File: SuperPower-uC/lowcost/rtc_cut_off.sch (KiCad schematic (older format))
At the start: 12 parts, among them Q1 2N7002, U7 PCF8563T, U8 XC6206P332MR, U9 TCA6408A, Y2 32.768KHz

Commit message: changed int io to directely connect to int bus
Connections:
- wire segments 59 -> 56
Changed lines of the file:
@@
 Text GLabel 5950 3550 2    50   Input ~ 0
 exp4
-Text GLabel 4550 3050 0    50   Input ~ 0
+Text GLabel 3750 2900 0    50   Input ~ 0
 INT_IO
 Wire Wire Line
@@
 Wire Wire Line
 	4650 3250 5100 3250
-Wire Wire Line
-	4550 3050 4600 3050
-Wire Wire Line
-	4600 3050 4600 3150
 Text GLabel 4650 3250 0    50   Input ~ 0
 3v3_EN
@@
 	1    0    0    -1
 $EndComp
-Connection ~ 4600 3150
-Wire Wire Line
-	4600 3150 4250 3150
-Wire Wire Line
-	4600 3150 5100 3150
 Wire Wire Line
 	4750 3050 5100 3050
@@
 Text Label 5050 2750 2    50   ~ 0
 V_I2C
+Wire Wire Line
+	4250 3150 5100 3150
 $EndSCHEMATC

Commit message: connected espander address pin to VBAT
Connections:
- wire segments 56 -> 55
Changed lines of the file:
@@
 Wire Wire Line
 	5100 2850 5050 2850
-Wire Wire Line
-	5050 2850 5050 2950
-Wire Wire Line
-	5050 2950 5100 2950
 $Comp
 L power:GND #PWR0109
@@
 	5600 4750 6100 4750
 Connection ~ 6100 4750
-Connection ~ 5050 2850
 Text Label 1750 850  2    50   ~ 0
 SDA
@@
 Wire Wire Line
 	4250 3150 5100 3150
+Text Label 4900 2950 0    50   ~ 0
+VBAT
+Wire Wire Line
+	4900 2950 5100 2950
 $EndSCHEMATC

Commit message: connected vccd of io expander to 3v3 i2c and added bypass cap
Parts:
- added C22: 0.1µF, Capacitor_SMD:C_0603_1608Metric_Pad1.05x0.95mm_HandSolder, symbol Device:C
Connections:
- wire segments 55 -> 58
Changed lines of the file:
@@
 Wire Wire Line
 	5900 3050 6150 3050
-Text Label 6150 2850 2    50   ~ 0
-VBAT
-Wire Wire Line
-	5900 2850 6150 2850
 Text Label 8650 2900 2    50   ~ 0
 SDA
@@
 Wire Wire Line
 	4250 3150 5100 3150
-Text Label 4900 2950 0    50   ~ 0
-VBAT
-Wire Wire Line
-	4900 2950 5100 2950
+Wire Wire Line
+	5100 2950 5050 2950
+Wire Wire Line
+	5050 2950 5050 2850
+Connection ~ 5050 2850
+Text Label 6450 2850 2    50   ~ 0
+V_I2C
+$Comp
+L Device:C C22
+U 1 1 5FC9C8EC
+P 6450 3050
+F 0 "C22" H 6300 2950 50  0000 L CNN
+F 1 "0.1µF" H 6200 3150 50  0000 L CNN
+F 2 "Capacitor_SMD:C_0603_1608Metric_Pad1.05x0.95mm_HandSolder" H 6488 2900 50  0001 C CNN
+F 3 "~" H 6450 3050 50  0001 C CNN
+F 4 "C14858" H 6450 3050 50  0001 C CNN "LCSC"
+	1    6450 3050
+	-1   0    0    1
+$EndComp
+Wire Wire Line
+	5900 2850 6450 2850
+$Comp
+L power:GND #PWR?
+U 1 1 5FCA03ED
+P 6450 3250
+F 0 "#PWR?" H 6450 3000 50  0001 C CNN
+F 1 "GND" H 6455 3077 50  0000 C CNN
+F 2 "" H 6450 3250 50  0001 C CNN
+F 3 "" H 6450 3250 50  0001 C CNN
+	1    6450 3250
+	1    0    0    -1
+$EndComp
+Wire Wire Line
+	6450 3250 6450 3200
+Wire Wire Line
+	6450 2900 6450 2850
 $EndSCHEMATC

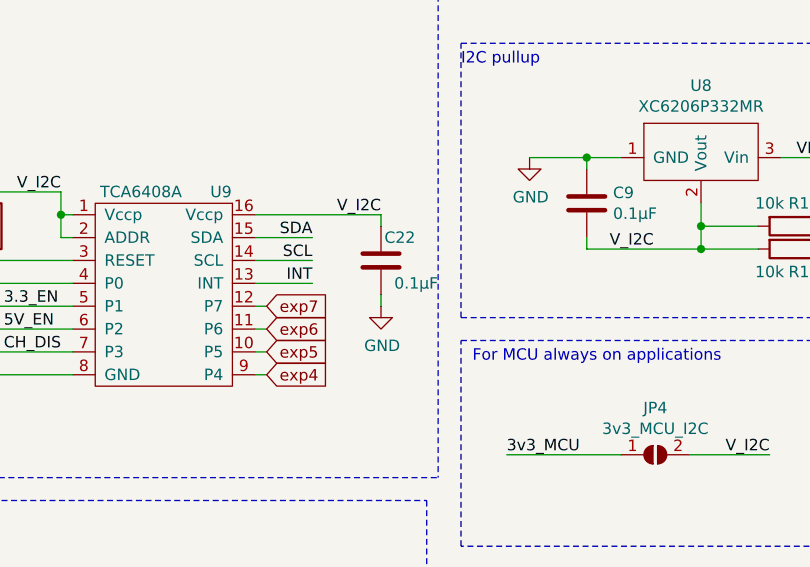
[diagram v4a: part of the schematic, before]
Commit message: added decoupling cap to io expander
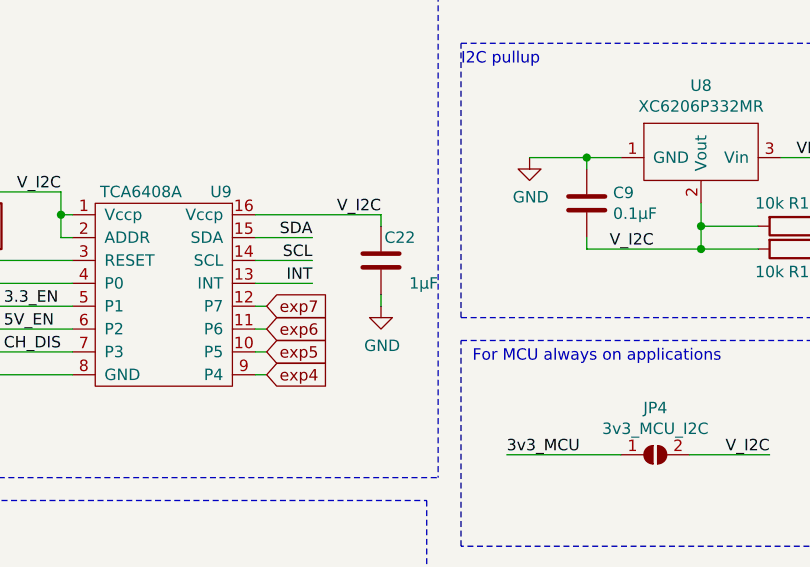
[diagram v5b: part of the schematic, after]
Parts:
- C22: value 0.1µF -> 1µF; LCSC C14858 -> C15849
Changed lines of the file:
@@
 P 6450 3050
 F 0 "C22" H 6300 2950 50  0000 L CNN
-F 1 "0.1µF" H 6200 3150 50  0000 L CNN
+F 1 "1µF" H 6200 3150 50  0000 L CNN
 F 2 "Capacitor_SMD:C_0603_1608Metric_Pad1.05x0.95mm_HandSolder" H 6488 2900 50  0001 C CNN
 F 3 "~" H 6450 3050 50  0001 C CNN
-F 4 "C14858" H 6450 3050 50  0001 C CNN "LCSC"
+F 4 "C15849" H 6450 3050 50  0001 C CNN "LCSC"
 	1    6450 3050
 	-1   0    0    1

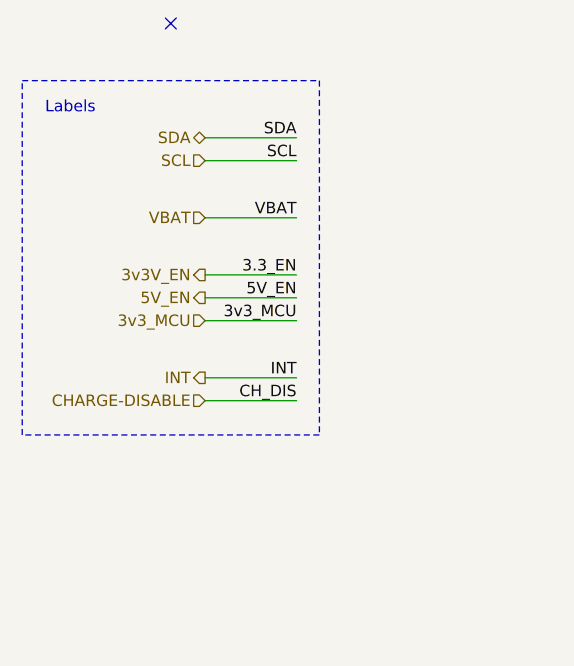
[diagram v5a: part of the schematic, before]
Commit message: added another gnd and 3v3_I2c to main pin header
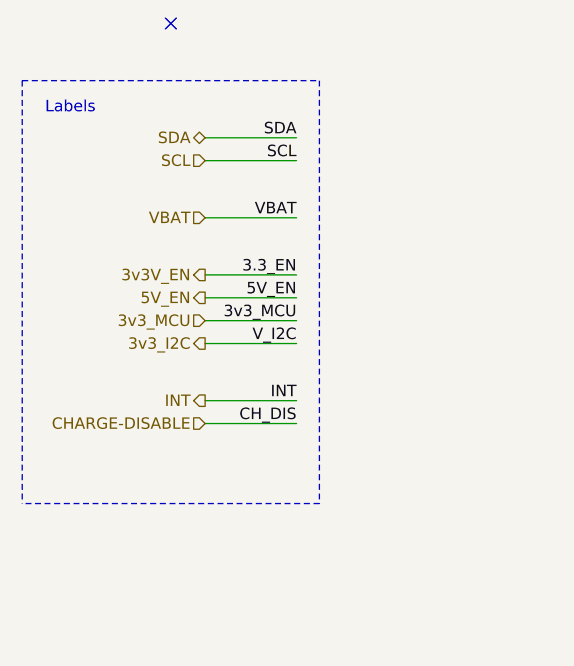
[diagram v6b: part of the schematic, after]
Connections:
- net labels added: 3v3_I2C
- wire segments 58 -> 59
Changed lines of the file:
@@
 Text HLabel 1350 1550 0    50   Output ~ 0
 5V_EN
-Text HLabel 1350 1900 0    50   Output ~ 0
+Text HLabel 1350 2000 0    50   Output ~ 0
 INT
 NoConn ~ 1200 350
@@
 Text Label 1750 1200 2    50   ~ 0
 VBAT
-Text Label 1750 1900 2    50   ~ 0
+Text Label 1750 2000 2    50   ~ 0
 INT
 Text Label 1750 1450 2    50   ~ 0
@@
 	5900 3150 6150 3150
 Wire Wire Line
-	1350 1900 1750 1900
+	1350 2000 1750 2000
 Wire Wire Line
 	1350 1550 1750 1550
@@
 Text Notes 3400 2000 0    50   ~ 0
 IO Expander
-Wire Notes Line
-	550  2150 550  600
-Text HLabel 1350 2000 0    50   Input ~ 0
+Text HLabel 1350 2100 0    50   Input ~ 0
 CHARGE-DISABLE
-Text Label 1750 2000 2    50   ~ 0
+Text Label 1750 2100 2    50   ~ 0
 CH_DIS
 Wire Wire Line
-	1750 2000 1350 2000
+	1750 2100 1350 2100
 Wire Notes Line
 	6800 3400 8450 3400
@@
 	550  600  1850 600
 Wire Notes Line
-	1850 600  1850 2150
-Wire Notes Line
-	1850 2150 550  2150
+	1850 2450 550  2450
 Text Label 7000 3900 0    50   ~ 0
 3v3_MCU
@@
 Wire Wire Line
 	6450 2900 6450 2850
+Wire Notes Line
+	1850 600  1850 2450
+Wire Notes Line
+	550  600  550  2450
+Text HLabel 1350 1750 0    50   Output ~ 0
+3v3_I2C
+Wire Wire Line
+	1350 1750 1750 1750
+Text Label 1750 1750 2    50   ~ 0
+V_I2C
 $EndSCHEMATC

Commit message: removed INT tp and improved routing a bit
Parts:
- removed TP2: TestPoint, TestPoint:TestPoint_Pad_1.5x1.5mm, symbol Connector:TestPoint
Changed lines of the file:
@@
 Wire Notes Line
 	6700 1850 6700 4000
-$Comp
-L Connector:TestPoint TP2
-U 1 1 5F96E9B6
-P 3950 2900
-F 0 "TP2" H 4008 3018 50  0000 L CNN
-F 1 "TestPoint" H 4008 2927 50  0000 L CNN
-F 2 "TestPoint:TestPoint_Pad_1.5x1.5mm" H 4150 2900 50  0001 C CNN
-F 3 "~" H 4150 2900 50  0001 C CNN
-	1    3950 2900
-	1    0    0    -1
-$EndComp
-Connection ~ 3950 2900
 Wire Wire Line
 	5950 3250 5900 3250
@@
 Text GLabel 5950 3550 2    50   Input ~ 0
 exp4
-Text GLabel 3750 2900 0    50   Input ~ 0
-INT_IO
 Wire Wire Line
 	4650 3450 5100 3450
@@
 Text Label 1750 1750 2    50   ~ 0
 V_I2C
+Text GLabel 3750 2900 0    50   Input ~ 0
+INT_IO
 $EndSCHEMATC

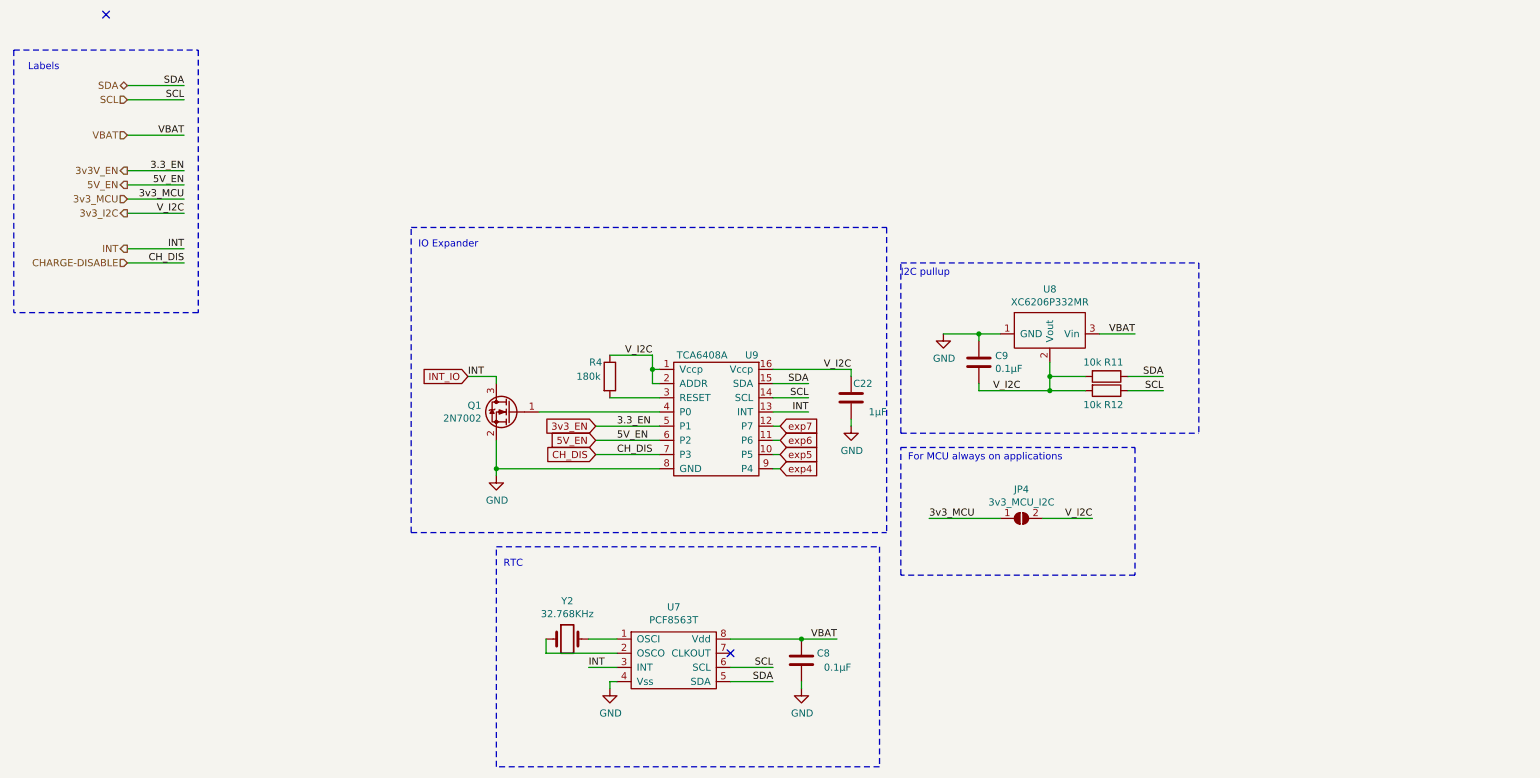
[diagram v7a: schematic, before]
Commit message: comments and optimisation
added some comments to the schematic swapped the CHARGE_DISABLE pin for another GND pin
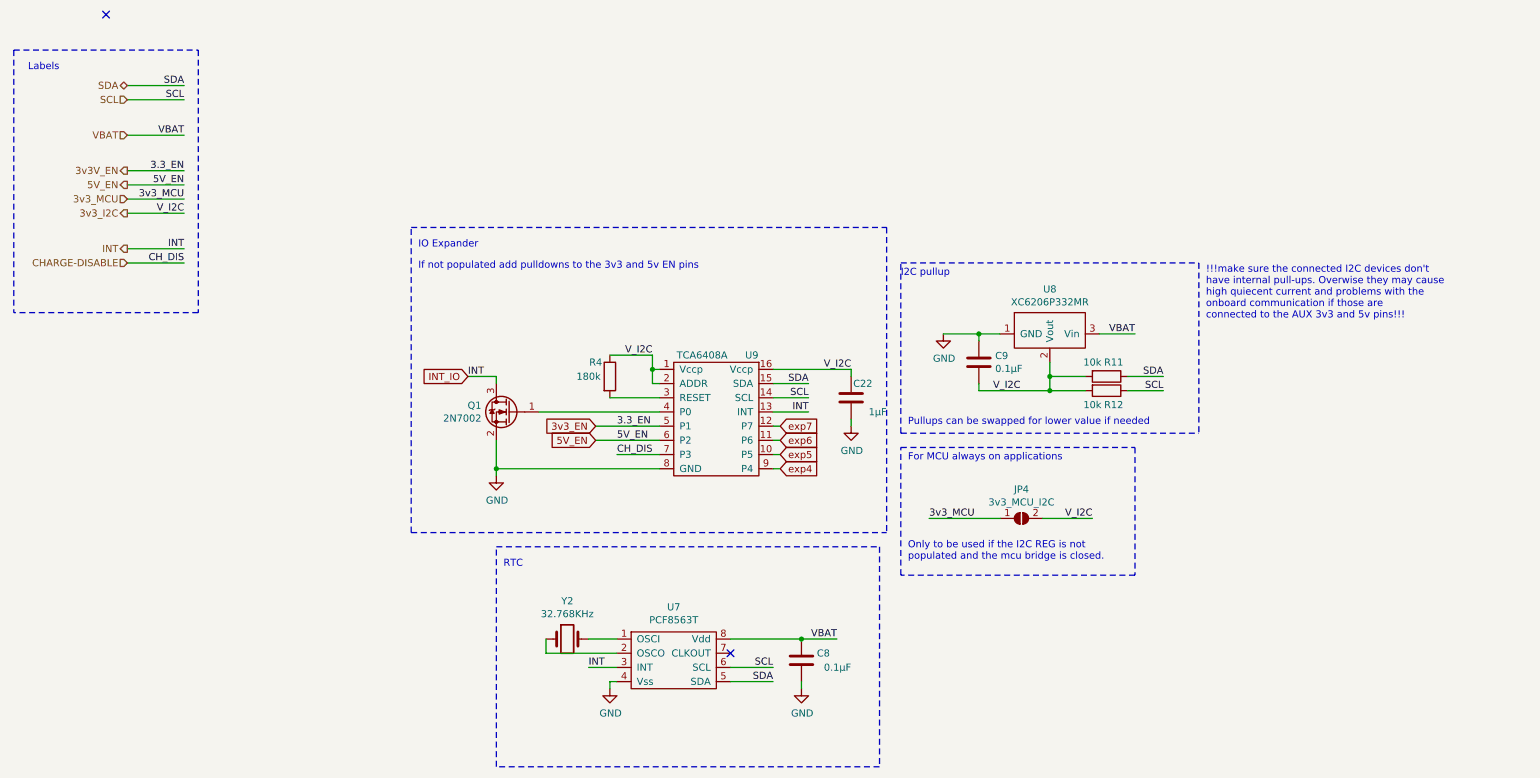
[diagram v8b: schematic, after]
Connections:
- net CH_DIS renamed CHARGE-DISABLE
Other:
- note added: "!!!make sure the connected I2C devices don't\nhave internal pull-ups. Overwise they may cause\nhigh quiecent current and problems with the\nonboard communication if those are\nconnected to the AUX 3v3 and 5v pins!!!"
- note added: "If not populated add pulldowns to the 3v3 and 5v EN pins"
- note added: "Only to be used if the I2C REG is not\npopulated and the mcu bridge is closed."
- note added: "Pullups can be swapped for lower value if needed"
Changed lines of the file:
@@
 exp4
 Wire Wire Line
-	4650 3450 5100 3450
+	4800 3450 5100 3450
 Wire Wire Line
 	4650 3350 5100 3350
@@
 Text GLabel 4650 3350 0    50   Input ~ 0
 5V_EN
-Text GLabel 4650 3450 0    50   Input ~ 0
-CH_DIS
 Text Label 4800 3250 0    50   ~ 0
 3.3_EN
@@
 Text GLabel 3750 2900 0    50   Input ~ 0
 INT_IO
+Text Notes 3400 2150 0    50   ~ 0
+If not populated add pulldowns to the 3v3 and 5v EN pins
+Text Notes 6850 3250 0    50   ~ 0
+Pullups can be swapped for lower value if needed
+Text Notes 8950 2500 0    50   ~ 0
+!!!make sure the connected I2C devices don't\nhave internal pull-ups. Overwise they may cause\nhigh quiecent current and problems with the\nonboard communication if those are\nconnected to the AUX 3v3 and 5v pins!!!
+Text Notes 6850 4200 0    50   ~ 0
+Only to be used if the I2C REG is not\npopulated and the mcu bridge is closed.
 $EndSCHEMATC
